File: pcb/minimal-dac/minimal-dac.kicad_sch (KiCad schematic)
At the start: 0 parts

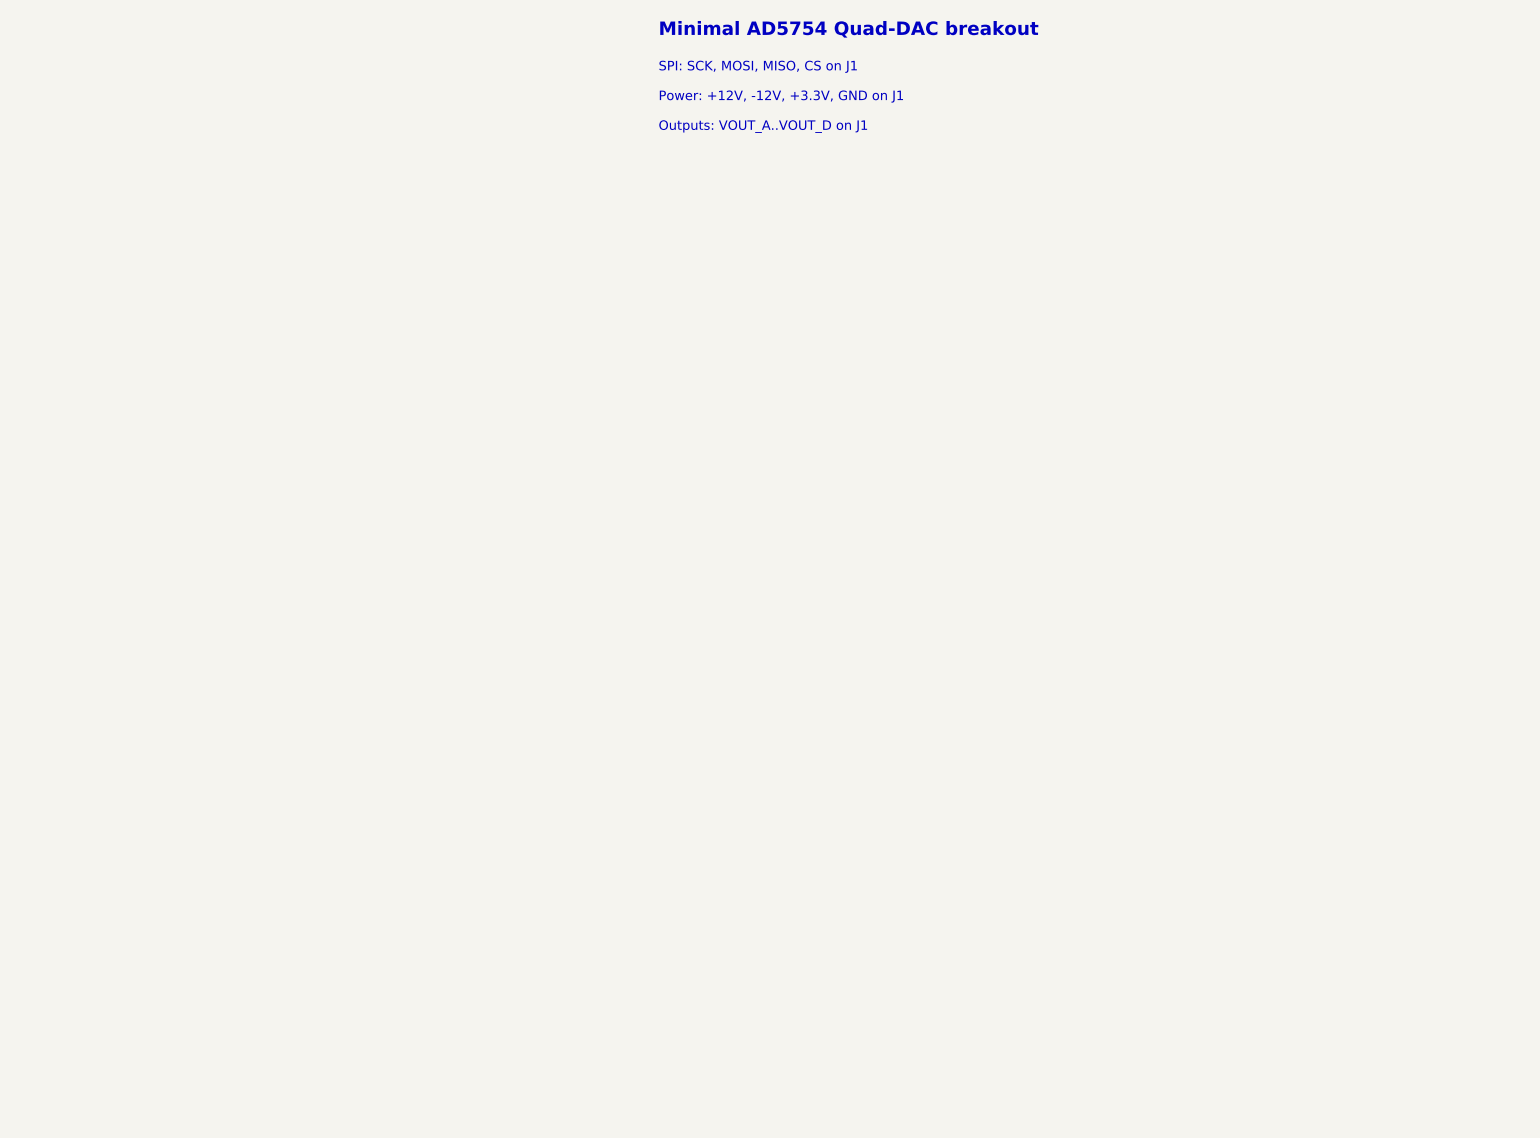
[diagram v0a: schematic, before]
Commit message: AD5754 pcb en elements gedachten
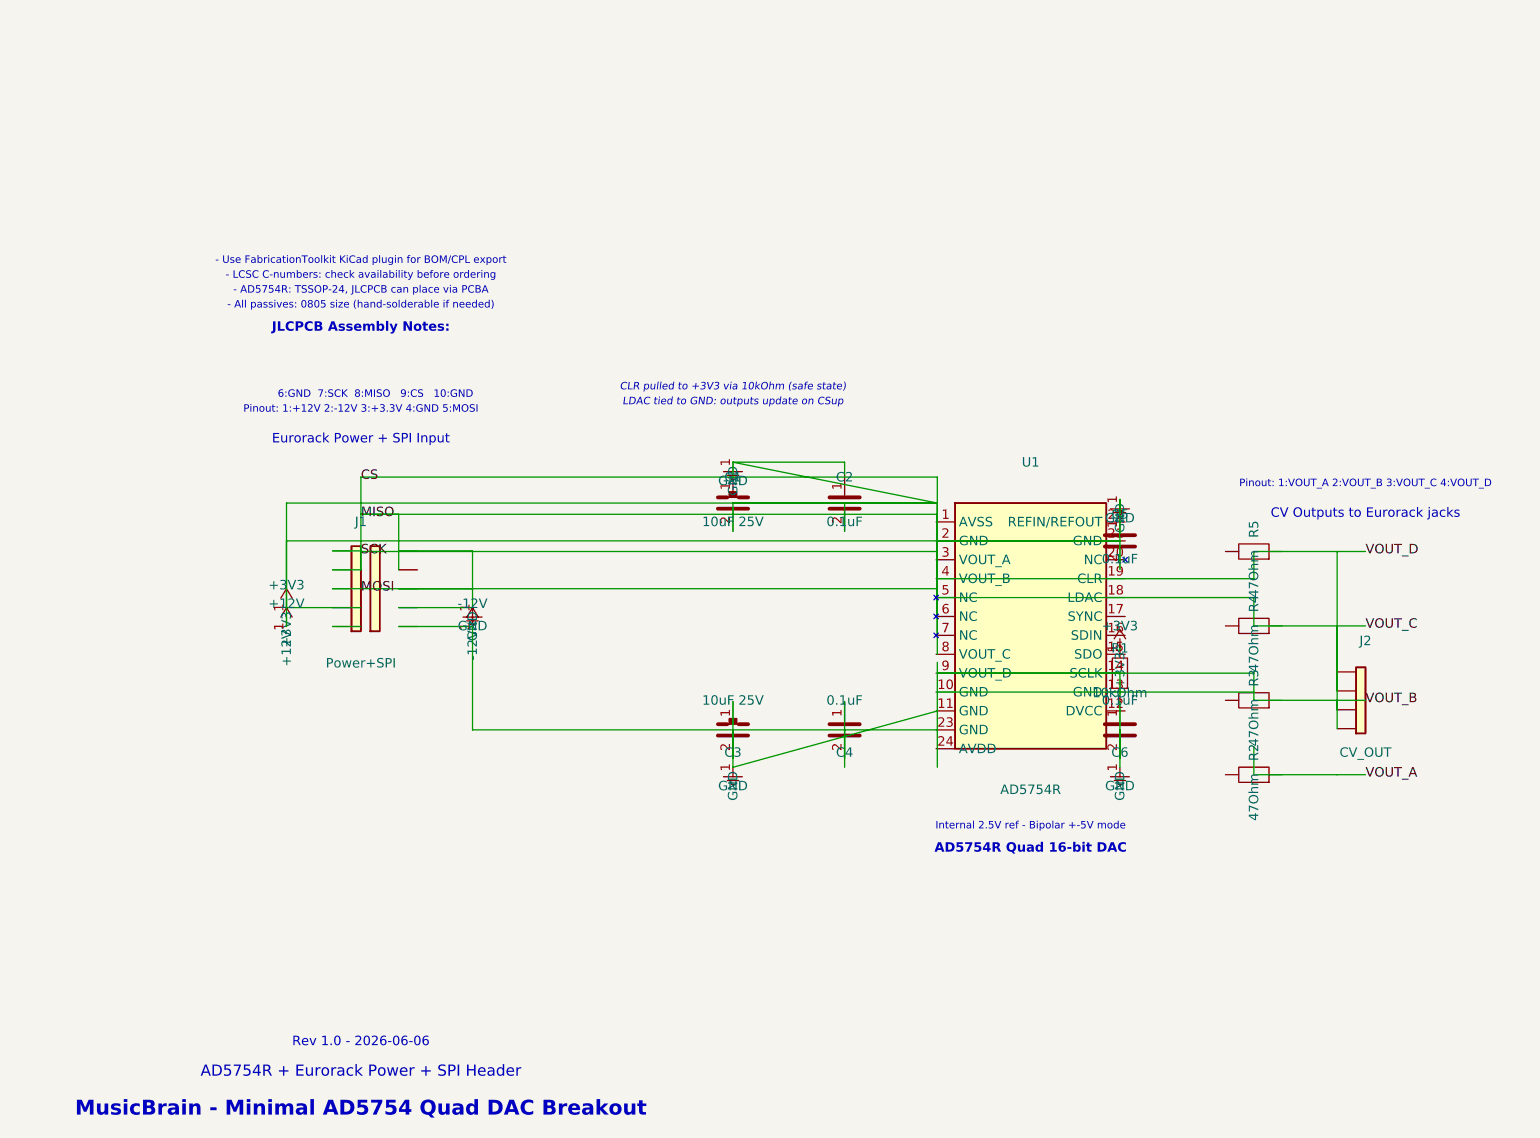
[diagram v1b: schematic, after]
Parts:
- added C1, C3: 10uF 25V, Capacitor_SMD:C_0805_2012Metric, symbol Device:CP
- added C2, C4, C5, C6: 0.1uF, Capacitor_SMD:C_0805_2012Metric, symbol Device:C
- added J1: Power+SPI, Connector_PinHeader_2.54mm:PinHeader_2x05_P2.54mm_Vertical, symbol Connector_Generic:Conn_02x05_Odd_Even
- added J2: CV_OUT, Connector_PinHeader_2.54mm:PinHeader_1x04_P2.54mm_Vertical, symbol Connector_Generic:Conn_01x04
- added R1: 10kOhm, Resistor_SMD:R_0805_2012Metric, symbol Device:R
- added R2, R3, R4, R5: 47Ohm, Resistor_SMD:R_0805_2012Metric, symbol Device:R
- added U1: AD5754R, Package_SO:TSSOP-24_4.4x7.8mm_P0.65mm, symbol Custom:AD5754R
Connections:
- new net: C3.1, C3.2, J1.10 (Pin_10)
- new net: C4.1, C4.2
- new net: C6.1, C6.2, R1.2
- new net CS: C1.1, C1.2, C2.1, C5.1, C5.2, J1.1 (Pin_1), J1.2 (Pin_2), J1.3 (Pin_3), J1.4 (Pin_4), J1.5 (Pin_5), J1.6 (Pin_6), J1.7 (Pin_7), J1.8 (Pin_8), J2.2 (Pin_2), J2.3 (Pin_3), J2.4 (Pin_4)
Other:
- note added: "- AD5754R: TSSOP-24, JLCPCB can place via PCBA"
- note added: "- All passives: 0805 size (hand-solderable if needed)"
- note added: "- LCSC C-numbers: check availability before ordering"
- note added: "- Use FabricationToolkit KiCad plugin for BOM/CPL export"
- note added: "6:GND 7:SCK 8:MISO 9:CS 10:GND"
- note added: "AD5754R + Eurorack Power + SPI Header"
- note added: "AD5754R Quad 16-bit DAC"
- note added: "CLR pulled to +3V3 via 10kOhm (safe state)"
- note added: "CV Outputs to Eurorack jacks"
- note added: "Eurorack Power + SPI Input"
- note added: "Internal 2.5V ref - Bipolar +-5V mode"
- note added: "JLCPCB Assembly Notes:"
- note added: "LDAC tied to GND: outputs update on CSup"
- note added: "MusicBrain - Minimal AD5754 Quad DAC Breakout"
- note added: "Pinout: 1:+12V 2:-12V 3:+3.3V 4:GND 5:MOSI"
- note added: "Pinout: 1:VOUT_A 2:VOUT_B 3:VOUT_C 4:VOUT_D"
- note added: "Rev 1.0 - 2026-06-06"
- note removed: "Minimal AD5754 Quad-DAC breakout"
- note removed: "Outputs: VOUT_A..VOUT_D on J1"
- note removed: "Power: +12V, -12V, +3.3V, GND on J1"
- note removed: "SPI: SCK, MOSI, MISO, CS on J1"
- company: MusicBrain -> (none)
- title: MusicBrain Minimal AD5754 Quad-DAC Breakout -> (none)

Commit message: pcbs
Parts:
- U1: value AD5754R -> AD5754BREZ; symbol Custom:AD5754R -> Custom:AD5754BREZ
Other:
- note added: "- AD5754BREZ: TSSOP-24, JLCPCB can place via PCBA"
- note added: "AD5754BREZ + Eurorack Power + SPI Header"
- note added: "AD5754BREZ Quad 16-bit DAC"
- note removed: "- AD5754R: TSSOP-24, JLCPCB can place via PCBA"
- note removed: "AD5754R + Eurorack Power + SPI Header"
- note removed: "AD5754R Quad 16-bit DAC"
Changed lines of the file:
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@@
   (text "MusicBrain - Minimal AD5754 Quad DAC Breakout" (at 30 165 0)
     (effects (font (size 2.0 2.0) (bold yes))))
-  (text "AD5754R + Eurorack Power + SPI Header" (at 30 160 0)
+  (text "AD5754BREZ + Eurorack Power + SPI Header" (at 30 160 0)
     (effects (font (size 1.5 1.5))))
   (text "Rev 1.0 - 2026-06-06" (at 30 156 0)
     (effects (font (size 1.27 1.27))))
-  (symbol (lib_id "Custom:AD5754R") (at 120 100 0) (unit 1)
+  (symbol (lib_id "Custom:AD5754BREZ") (at 120 100 0) (unit 1)
     (in_bom yes) (on_board yes) (uuid "qdac0001-0001-0001-0001-000000000001")
     (property "Reference" "U1" (at 120 78 0) (effects (font (size 1.27 1.27))))
-    (property "Value" "AD5754R" (at 120 122 0) (effects (font (size 1.27 1.27))))
+    (property "Value" "AD5754BREZ" (at 120 122 0) (effects (font (size 1.27 1.27))))
     (property "Footprint" "Package_SO:TSSOP-24_4.4x7.8mm_P0.65mm" (at 0 0 0)
       (effects (font (size 1.27 1.27)) (hide yes)))
-    (property "Datasheet" "https://www.analog.com/media/en/technical-documentation/data-sheets/AD5754R.pdf" (at 0 0 0)
+    (property "Datasheet" "https://www.analog.com/media/en/technical-documentation/data-sheets/AD5754.pdf" (at 0 0 0)
       (effects (font (size 1.27 1.27)) (hide yes)))
   )
@@
   (text "CV Outputs to Eurorack jacks" (at 165 85 0) (effects (font (size 1.27 1.27))))
   (text "Pinout: 1:VOUT_A 2:VOUT_B 3:VOUT_C 4:VOUT_D" (at 165 81 0) (effects (font (size 1.0 1.0))))
-  (text "AD5754R Quad 16-bit DAC" (at 120 130 0) (effects (font (size 1.27 1.27) (bold yes))))
+  (text "AD5754BREZ Quad 16-bit DAC" (at 120 130 0) (effects (font (size 1.27 1.27) (bold yes))))
   (text "Internal 2.5V ref - Bipolar +-5V mode" (at 120 127 0) (effects (font (size 1.0 1.0))))
   (text "LDAC tied to GND: outputs update on CSup" (at 80 70 0) (effects (font (size 1.0 1.0) (italic yes))))
@@
   (text "JLCPCB Assembly Notes:" (at 30 60 0) (effects (font (size 1.27 1.27) (bold yes))))
   (text "- All passives: 0805 size (hand-solderable if needed)" (at 30 57 0) (effects (font (size 1.0 1.0))))
-  (text "- AD5754R: TSSOP-24, JLCPCB can place via PCBA" (at 30 55 0) (effects (font (size 1.0 1.0))))
+  (text "- AD5754BREZ: TSSOP-24, JLCPCB can place via PCBA" (at 30 55 0) (effects (font (size 1.0 1.0))))
   (text "- LCSC C-numbers: check availability before ordering" (at 30 53 0) (effects (font (size 1.0 1.0))))
   (text "- Use FabricationToolkit KiCad plugin for BOM/CPL export" (at 30 51 0) (effects (font (size 1.0 1.0))))
